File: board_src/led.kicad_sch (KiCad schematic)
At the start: 17 parts, among them J2 Conn_01x08

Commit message: wersja 3d
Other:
- note added: "uaktualnić footprinty"
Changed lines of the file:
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@@
+		)
+	)
+	(text "uaktualnić footprinty"
+		(exclude_from_sim no)
+		(at 140.462 107.696 0)
+		(effects
+			(font
+				(size 1.27 1.27)
+			)
 		)
 	)

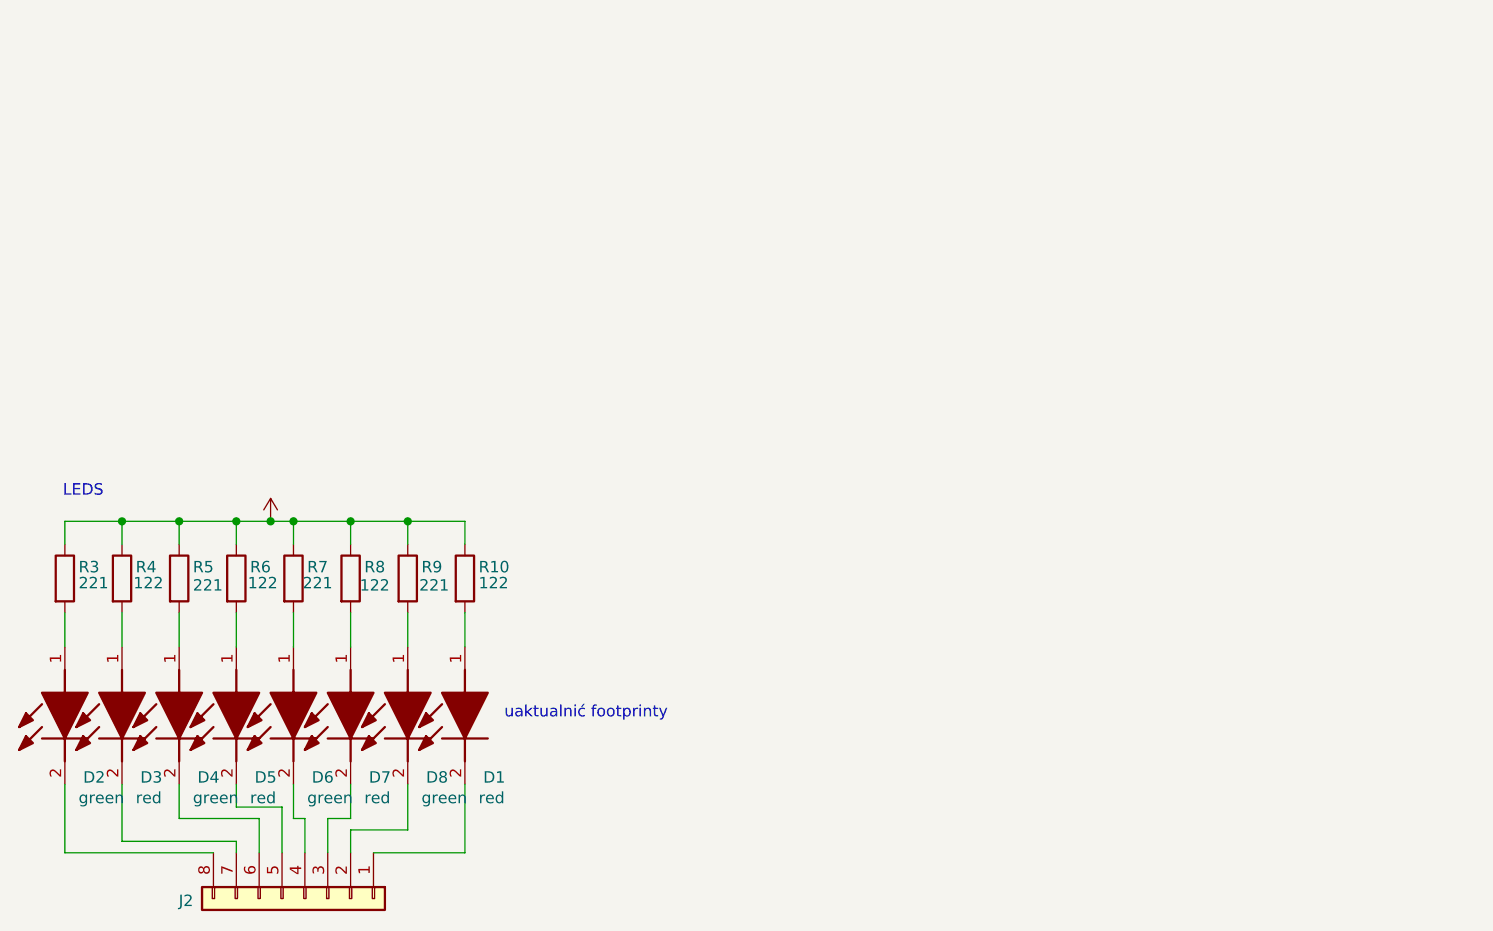
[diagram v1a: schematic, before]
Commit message: wersja z wyswietlaczem LCD
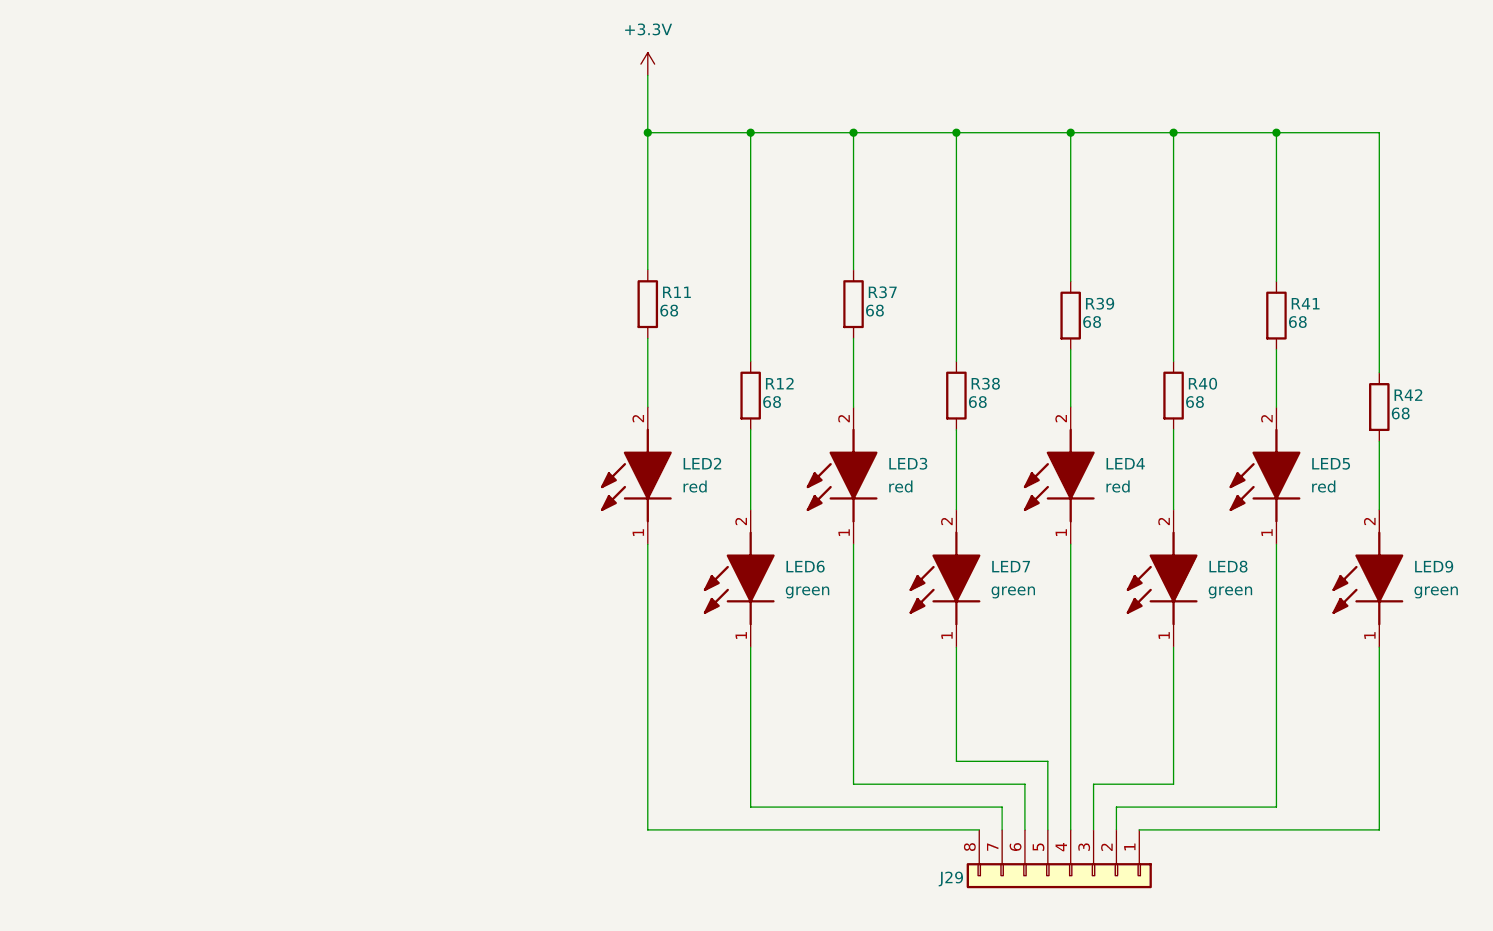
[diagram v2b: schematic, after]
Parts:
- removed D1, D3, D5, D7: red, footprints:L128GRN2003500000, symbol L128-GRN2003500000:L128-GRN2003500000
- removed D2, D4, D6, D8: green, footprints:L128GRN2003500000, symbol L128-GRN2003500000:L128-GRN2003500000
- removed J2: Conn_01x08, Connector_PinHeader_2.54mm:PinHeader_1x08_P2.54mm_Vertical, symbol Connector_Generic:Conn_01x08
- removed R10, R4, R6, R8: 122, Resistor_SMD:R_0201_0603Metric, symbol Device:R
- removed R3, R5, R7, R9: 221, Resistor_SMD:R_0201_0603Metric, symbol Device:R
- added J29: Conn_01x08, Connector_PinHeader_2.54mm:PinHeader_1x08_P2.54mm_Vertical, symbol Connector_Generic:Conn_01x08
- added LED2, LED3, LED4, LED5: red, footprints:LEDC1608X80N, symbol LS_Q976-NR-1:LS_Q976-NR-1
- added LED6, LED7, LED8, LED9: green, footprints:LEDC1608X100N, symbol VLMTG1300-GS08:VLMTG1300-GS08
- added R11, R12, R37, R38, R39, R40, R41, R42: 68, Resistor_SMD:R_0201_0603Metric, symbol Device:R
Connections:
- net +3.3V: now also R11.1, R12.1, R37.1, R38.1, R39.1, R40.1, R41.1, R42.1
- new net: J29.1 (Pin_1), LED9.1 (K)
- new net: J29.2 (Pin_2), LED5.1 (K)
- new net: J29.3 (Pin_3), LED8.1 (K)
- new net: J29.4 (Pin_4), LED4.1 (K)
- new net: J29.5 (Pin_5), LED7.1 (K)
- new net: J29.6 (Pin_6), LED3.1 (K)
- new net: J29.7 (Pin_7), LED6.1 (K)
- new net: J29.8 (Pin_8), LED2.1 (K)
- new net: LED9.2 (A), R42.2
- new net: LED8.2 (A), R40.2
- new net: LED2.2 (A), R11.2
- new net: LED4.2 (A), R39.2
- new net: LED3.2 (A), R37.2
- new net: LED7.2 (A), R38.2
- new net: LED5.2 (A), R41.2
- new net: LED6.2 (A), R12.2
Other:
- note removed: "LEDS"
- note removed: "uaktualnić footprinty"

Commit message: wersja z FT232RN
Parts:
- R11, R12, R37, R38, R39, R40, R41, R42: footprint Resistor_SMD:R_0201_0603Metric -> Resistor_SMD:R_1206_3216Metric
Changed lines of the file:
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@@
 			)
 		)
-		(property "Footprint" "Resistor_SMD:R_0201_0603Metric"
+		(property "Footprint" "Resistor_SMD:R_1206_3216Metric"
 			(at 226.822 73.66 90)
 			(effects
@@
 			)
 		)
-		(property "Footprint" "Resistor_SMD:R_0201_0603Metric"
+		(property "Footprint" "Resistor_SMD:R_1206_3216Metric"
 			(at 203.962 72.39 90)
 			(effects
@@
 			)
 		)
-		(property "Footprint" "Resistor_SMD:R_0201_0603Metric"
+		(property "Footprint" "Resistor_SMD:R_1206_3216Metric"
 			(at 168.402 62.23 90)
 			(effects
@@
 			)
 		)
-		(property "Footprint" "Resistor_SMD:R_0201_0603Metric"
+		(property "Footprint" "Resistor_SMD:R_1206_3216Metric"
 			(at 145.542 62.23 90)
 			(effects
@@
 			)
 		)
-		(property "Footprint" "Resistor_SMD:R_0201_0603Metric"
+		(property "Footprint" "Resistor_SMD:R_1206_3216Metric"
 			(at 192.532 63.5 90)
 			(effects
@@
 			)
 		)
-		(property "Footprint" "Resistor_SMD:R_0201_0603Metric"
+		(property "Footprint" "Resistor_SMD:R_1206_3216Metric"
 			(at 179.832 72.39 90)
 			(effects
@@
 			)
 		)
-		(property "Footprint" "Resistor_SMD:R_0201_0603Metric"
+		(property "Footprint" "Resistor_SMD:R_1206_3216Metric"
 			(at 215.392 63.5 90)
 			(effects
@@
 			)
 		)
-		(property "Footprint" "Resistor_SMD:R_0201_0603Metric"
+		(property "Footprint" "Resistor_SMD:R_1206_3216Metric"
 			(at 156.972 72.39 90)
 			(effects

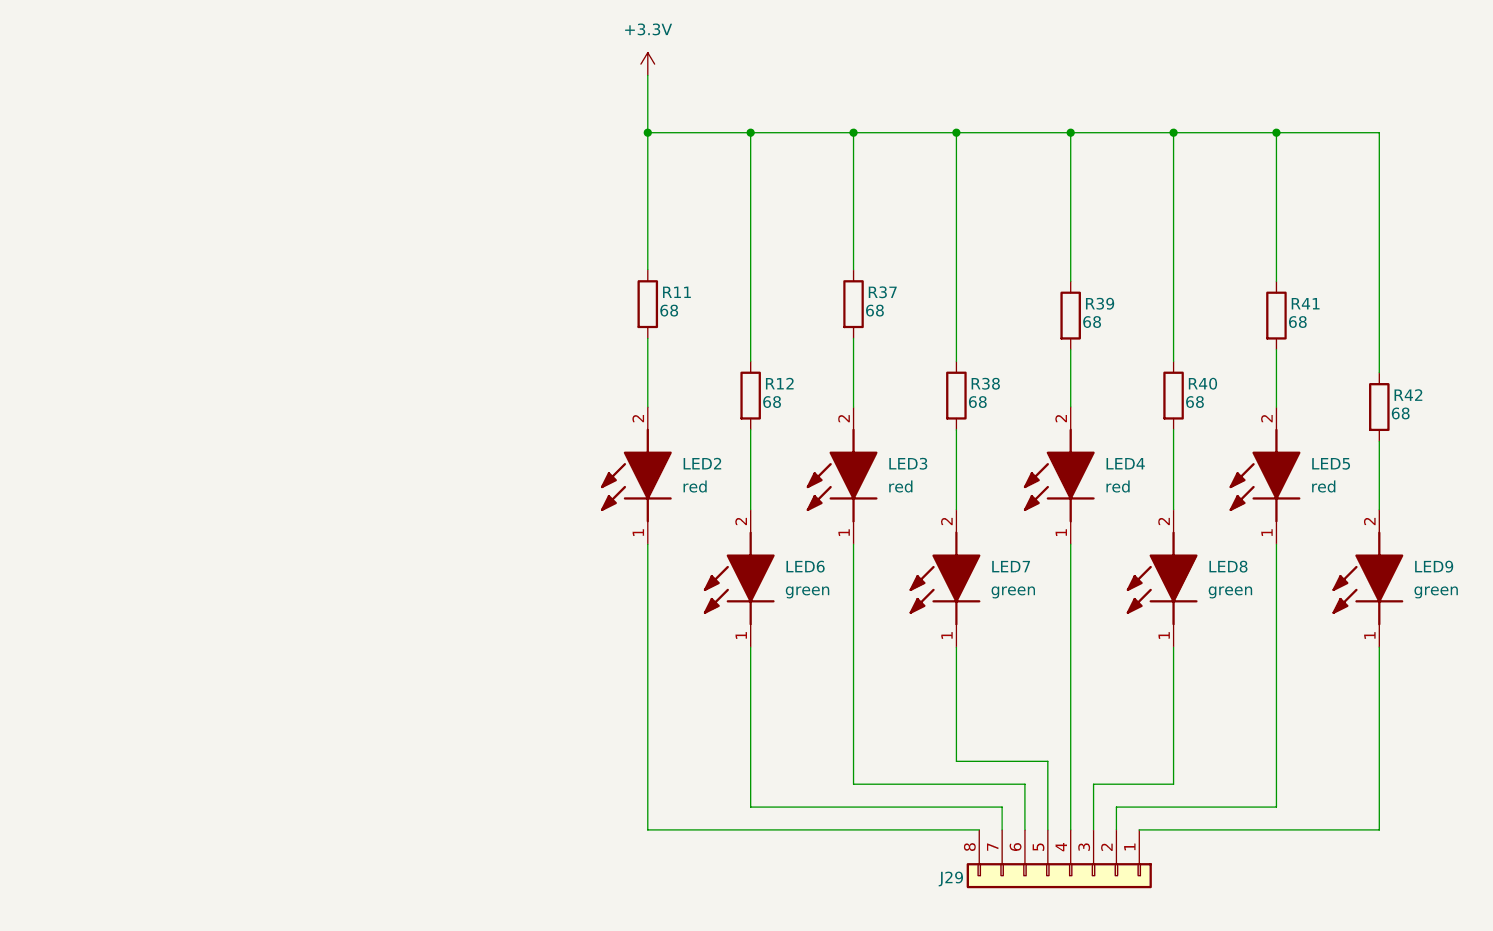
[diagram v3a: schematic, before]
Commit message: Wersja ze sciezkami miedzianymi
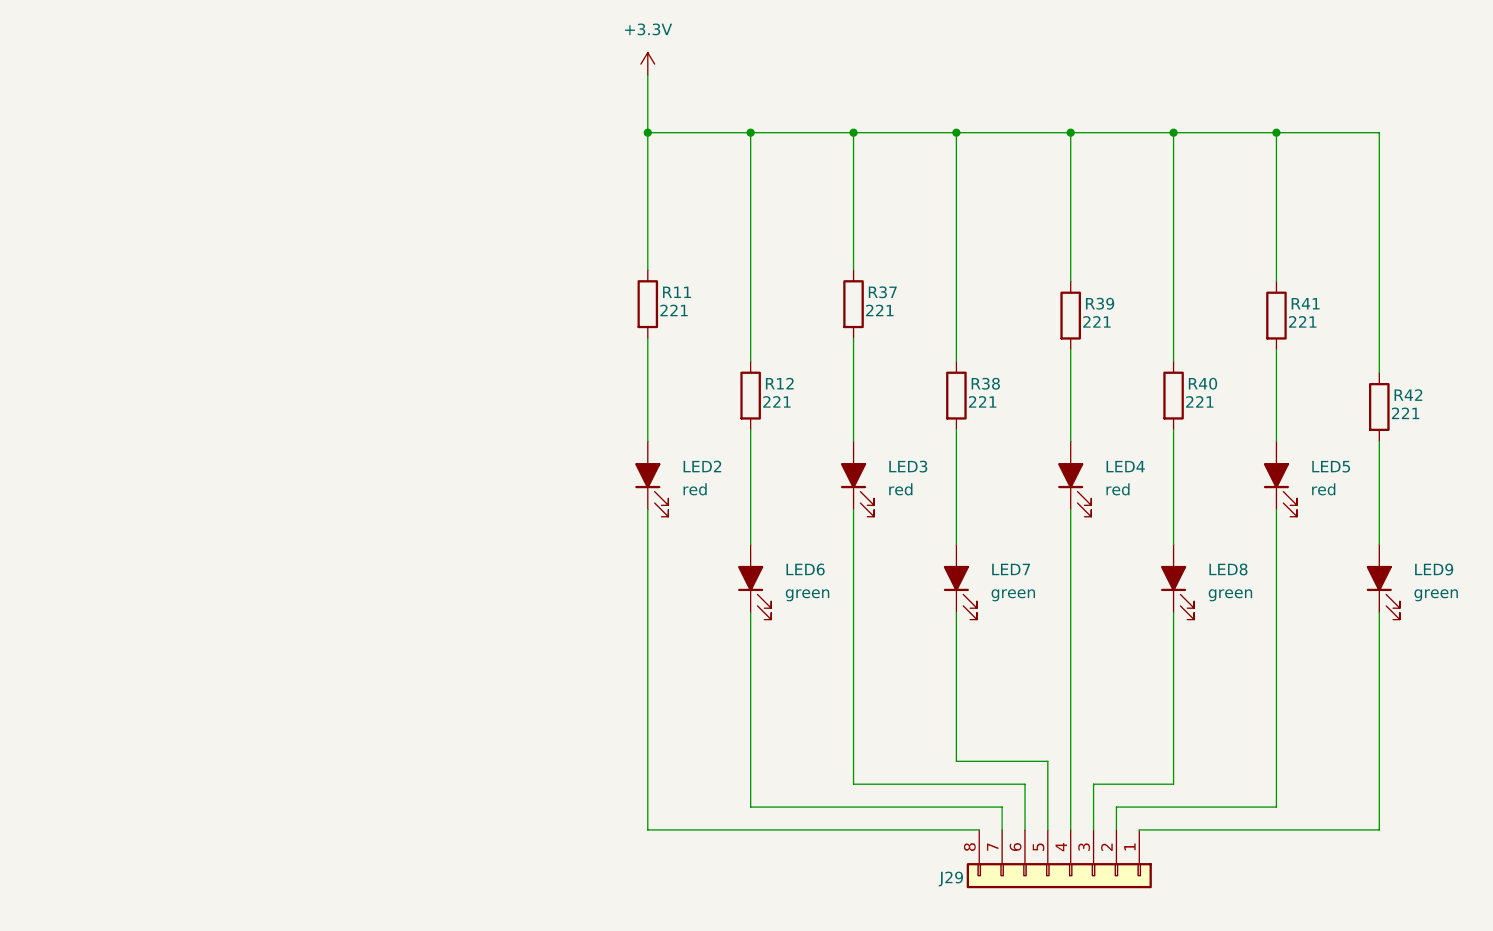
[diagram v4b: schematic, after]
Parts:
- LED2, LED3, LED4, LED5: symbol LS_Q976-NR-1:LS_Q976-NR-1 -> Device:LED_Filled
- LED6, LED7, LED8, LED9: symbol VLMTG1300-GS08:VLMTG1300-GS08 -> Device:LED_Filled
- R11, R12, R37, R38, R39, R40, R41, R42: value 68 -> 221; footprint Resistor_SMD:R_1206_3216Metric -> Resistor_SMD:R_0603_1608Metric

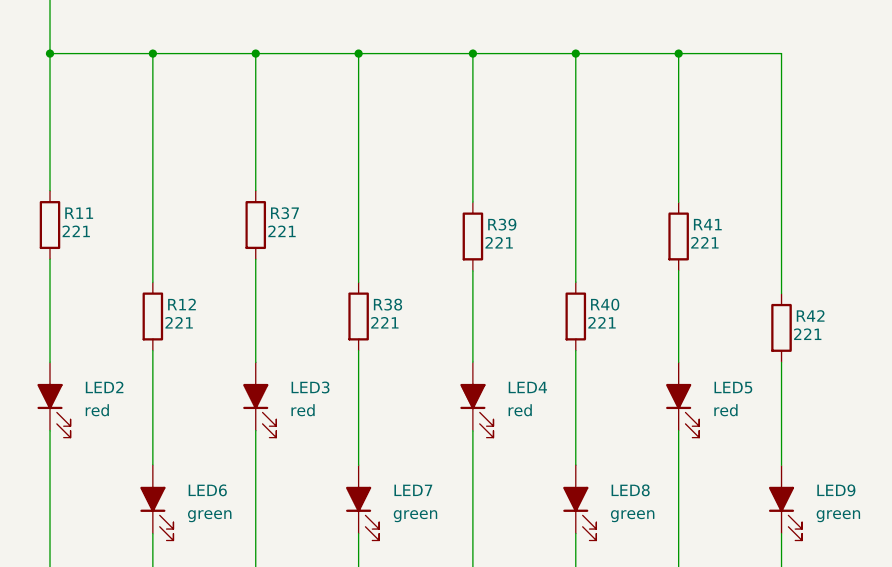
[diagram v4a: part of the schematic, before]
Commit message: poprawione polaczenia diod i wartosci opornikow, aktualizacja niektorych elementow ze wzgledu na braki w magazynie
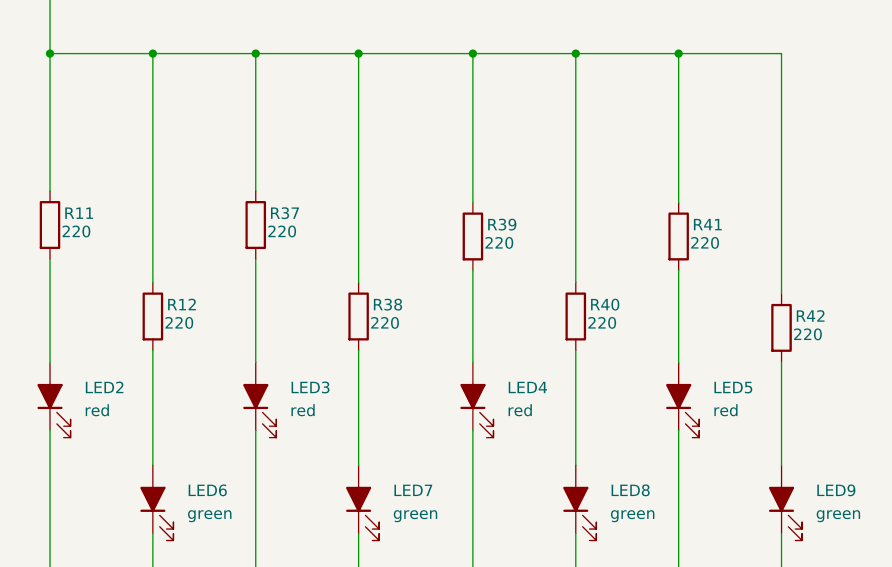
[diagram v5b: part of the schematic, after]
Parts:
- R11, R12, R37, R38, R39, R40, R41, R42: value 221 -> 220
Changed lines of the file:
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@@
 			)
 		)
-		(property "Value" "221"
+		(property "Value" "220"
 			(at 229.87 74.422 0)
 			(effects
@@
 			)
 		)
-		(property "Value" "221"
+		(property "Value" "220"
 			(at 207.01 73.152 0)
 			(effects
@@
 			)
 		)
-		(property "Value" "221"
+		(property "Value" "220"
 			(at 171.45 62.992 0)
 			(effects
@@
 			)
 		)
-		(property "Value" "221"
+		(property "Value" "220"
 			(at 148.59 62.992 0)
 			(effects
@@
 			)
 		)
-		(property "Value" "221"
+		(property "Value" "220"
 			(at 195.58 64.262 0)
 			(effects
@@
 			)
 		)
-		(property "Value" "221"
+		(property "Value" "220"
 			(at 182.88 73.152 0)
 			(effects
@@
 			)
 		)
-		(property "Value" "221"
+		(property "Value" "220"
 			(at 218.44 64.262 0)
 			(effects
@@
 			)
 		)
-		(property "Value" "221"
+		(property "Value" "220"
 			(at 160.02 73.152 0)
 			(effects
